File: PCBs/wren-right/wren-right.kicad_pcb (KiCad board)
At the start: 2 copper layers, 151.7 x 117 mm, 67 parts, among them J1 TRRS_Jack, SW0 Reset, U1 Elite C

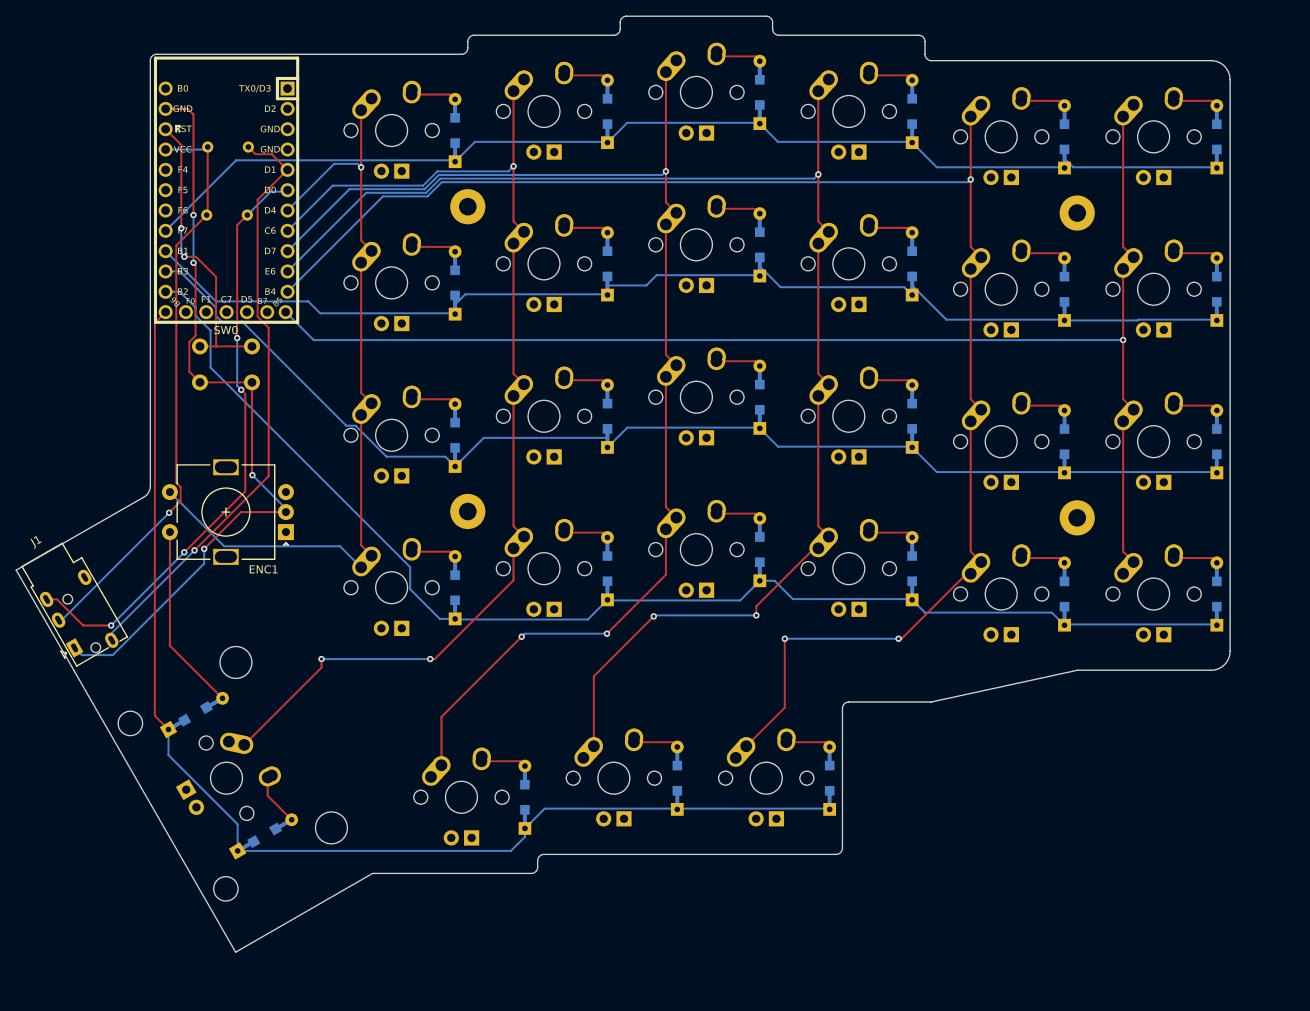
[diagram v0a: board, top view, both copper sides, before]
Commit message: Reposition Rotary Encoder and Create New Right Board
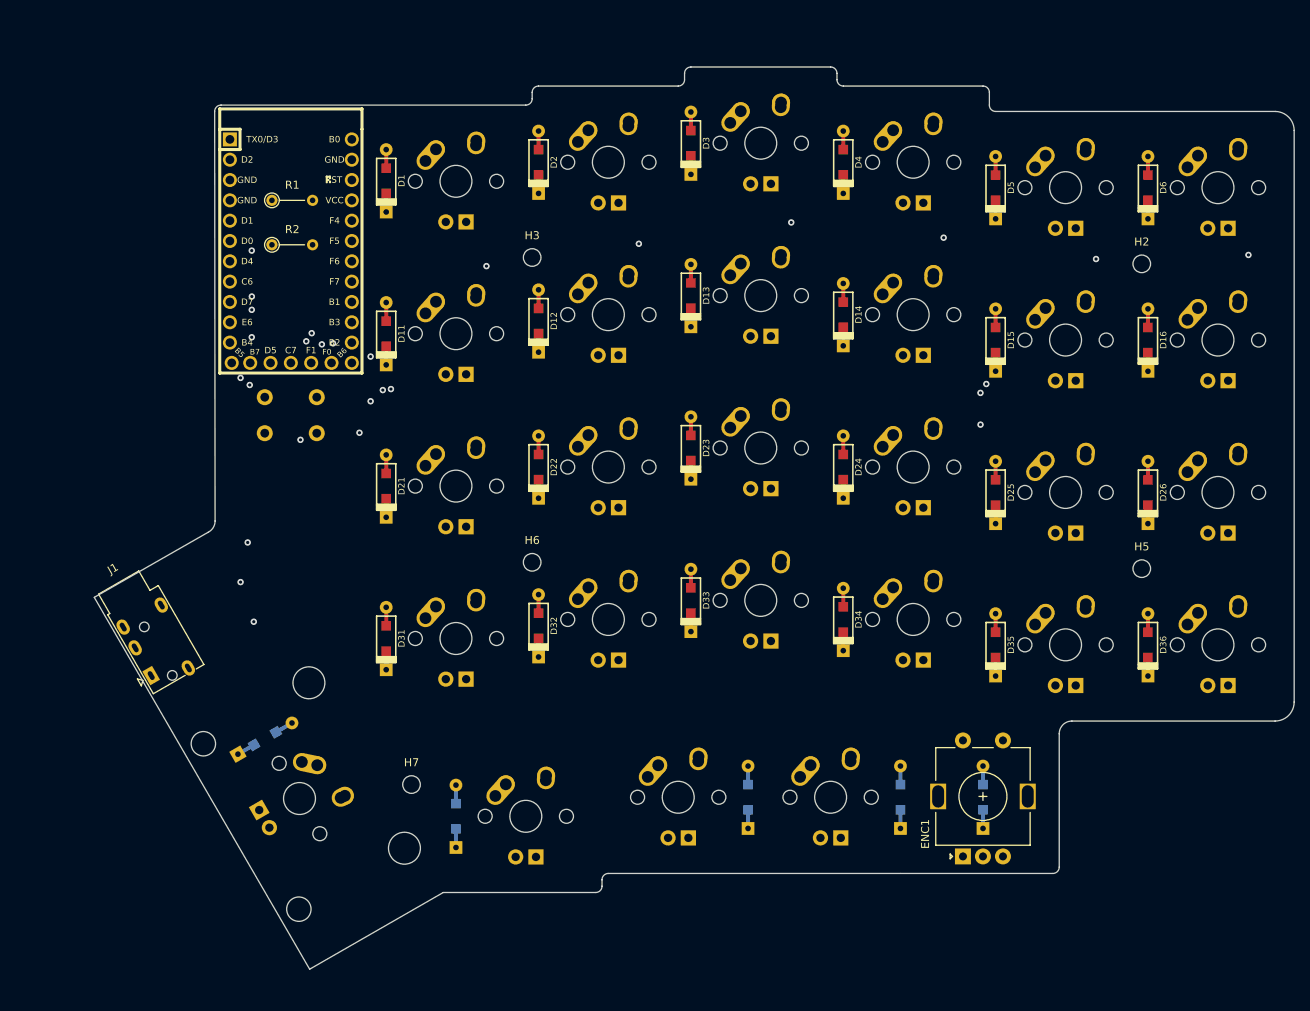
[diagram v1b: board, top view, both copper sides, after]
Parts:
- removed REF** (x4): MountingHole_2.2mm_M2_Pad, MountingHole:MountingHole_2.2mm_M2_Pad
- added H2: MountingHole, MountingHole:MountingHole_2.2mm_M2_ISO7380, F.Cu at (211.9, 73.0)
- added H3: MountingHole, MountingHole:MountingHole_2.2mm_M2_ISO7380, F.Cu at (135.7, 72.2)
- added H5: MountingHole, MountingHole:MountingHole_2.2mm_M2_ISO7380, F.Cu at (211.9, 111.1)
- added H6: MountingHole, MountingHole:MountingHole_2.2mm_M2_ISO7380, F.Cu at (135.7, 110.3)
- added H7: MountingHole, MountingHole:MountingHole_2.2mm_M2_ISO7380, F.Cu at (120.7, 138.1)
- D1, D11, D12, D13, D14, D15, D16, D2, D21, D22, D23, D24, D25, D26, D3, D31, D32, D33, D34, D35, D36, D4, D5, D6, R1, R2: moved to F.Cu
- U1: value Elite C -> Elite-C; moved to F.Cu
- moved ENC1 93.8 mm to (189.6, 147.1), turned to 90 degrees
- moved D44 28.0 mm to (181.8, 139.7)
- moved D43 27.9 mm to (162.7, 139.7)
- moved D42 24.0 mm to (126.2, 142.1), turned to 90 degrees
- moved D45 19.3 mm to (192.1, 139.7)
- moved D12 11.2 mm to (136.5, 80.2)
- moved D32 11.2 mm to (136.5, 118.3)
- moved D35 10.7 mm to (193.7, 120.7)
- moved D5 10.7 mm to (193.7, 63.5)
- moved D15 10.7 mm to (193.7, 82.5)
- moved D25 10.7 mm to (193.7, 101.6)
- moved D13 10.7 mm to (155.6, 77.0)
- moved D21 10.7 mm to (117.5, 100.8)
- moved D23 10.7 mm to (155.6, 96.0)
- moved D31 10.7 mm to (117.5, 119.9)
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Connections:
- D41 pad 2: ENC1-OUT -> Net-(D41-Pad2)
- D45 pad 2: Net-(D45-Pad2) -> ENC1-IN
- ENC1 pad A: (no net) -> LEFT
- ENC1 pad B: (no net) -> RIGHT
- ENC1 pad S1: COL0 -> ENC1-IN
- ENC1 pad S2: ENC1-OUT -> COL4
- MX41 pad 1: COL1 -> COL0
- MX41 pad 2: Net-(D42-Pad2) -> Net-(D41-Pad2)
- MX42 pad 1: COL2 -> COL1
- MX42 pad 2: Net-(D43-Pad2) -> Net-(D42-Pad2)
- MX43 pad 1: COL3 -> COL2
- MX43 pad 2: Net-(D44-Pad2) -> Net-(D43-Pad2)
- MX44 pad 1: COL4 -> COL3
- MX44 pad 2: Net-(D45-Pad2) -> Net-(D44-Pad2)
- U1 pad 1: (no net) -> ROW0
- U1 pad 10: COL3 -> COL9
- U1 pad 11: COL4 -> Net-(U1-Pad11)
- U1 pad 12: COL5 -> ROW4
- U1 pad 13: ROW4 -> COL0
- U1 pad 14: ROW3 -> COL1
- U1 pad 15: ROW2 -> COL2
- U1 pad 16: ROW1 -> COL3
- U1 pad 17: ROW0 -> COL4
- U1 pad 18: (no net) -> COL5
- U1 pad 19: (no net) -> COL6
- U1 pad 2: (no net) -> ROW1
- U1 pad 20: (no net) -> COL7
- U1 pad 24: (no net) -> Net-(U1-Pad24)
- U1 pad 25: (no net) -> Net-(U1-Pad25)
- U1 pad 26: (no net) -> Net-(U1-Pad26)
- U1 pad 27: (no net) -> Net-(U1-Pad27)
- U1 pad 28: (no net) -> RIGHT
- U1 pad 29: (no net) -> LEFT
- U1 pad 3: (no net) -> Net-(U1-Pad3)
- U1 pad 4: (no net) -> Net-(U1-Pad4)
- U1 pad 7: COL0 -> ROW2
- U1 pad 8: COL1 -> ROW3
- U1 pad 9: COL2 -> COL8
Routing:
- net COL4: track 187.6 -> 0.00 mm, vias 3 -> 1
- net COL3: track 169.9 -> 0.00 mm, vias 3 -> 1
- net COL5: track 160.5 -> 0.00 mm
- net ROW3: track 157.7 -> 0.00 mm
- net COL2: track 153.0 -> 0.00 mm, vias 3 -> 1
- net ROW4: track 149.1 -> 0.00 mm
- net ROW2: track 147.0 -> 0.00 mm, vias 0 -> 1
- net ROW0: track 140.5 -> 0.00 mm
- net ROW1: track 140.3 -> 0.00 mm, vias 0 -> 2
- net COL1: track 132.8 -> 0.00 mm, vias 3 -> 1
- net GND: track 98.0 -> 0.00 mm
- net COL0: track 94.0 -> 0.00 mm
- net SDA: track 75.1 -> 0.00 mm, vias 1 -> 2
- net SCL: track 74.9 -> 0.00 mm, vias 4 -> 3
- net VCC: track 72.9 -> 0.00 mm, vias 1 -> 4
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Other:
- board size 151.7 x 117 mm -> 150 x 112.8 mm

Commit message: Various Updates
New plates, updated routing on the right side, assorted other changes.
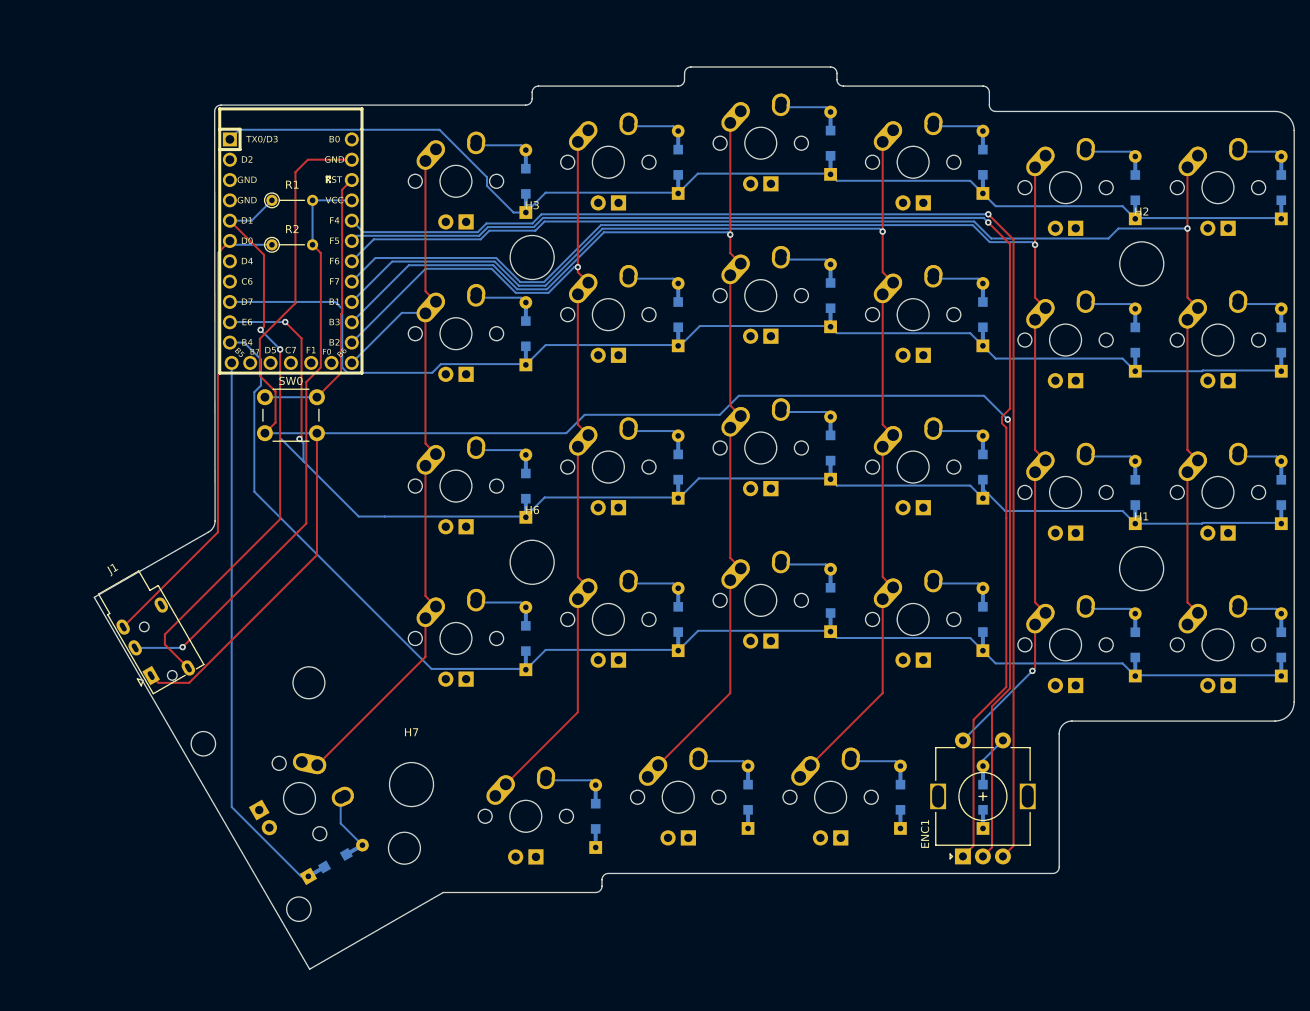
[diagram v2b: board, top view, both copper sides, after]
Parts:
- removed H5: MountingHole, MountingHole:MountingHole_2.2mm_M2_ISO7380
- added H1: MountingHole, MountingHole:MountingHole_5.5mm, F.Cu at (211.9, 111.1)
- D1, D11, D12, D13, D14, D15, D16, D2, D21, D22, D23, D24, D25, D26, D3, D31, D32, D33, D34, D35, D36, D4, D5, D6: moved to B.Cu
- H2, H3, H6, H7: footprint MountingHole:MountingHole_2.2mm_M2_ISO7380 -> MountingHole:MountingHole_5.5mm
- SW0: moved to F.Cu
- moved D41 17.6 mm to (111.1, 147.6)
- moved D12 17.5 mm to (154.0, 79.4)
- moved D32 17.5 mm to (154.0, 117.5)
- moved D42 17.5 mm to (143.7, 142.1)
- moved D1 17.5 mm to (134.9, 62.7)
- moved D15 17.5 mm to (211.1, 82.5)
- moved D25 17.5 mm to (211.1, 101.6)
- moved D35 17.5 mm to (211.1, 120.7)
- moved D5 17.5 mm to (211.1, 63.5)
- moved D11 17.5 mm to (134.9, 81.8)
- moved D13 17.5 mm to (173.0, 77.0)
- moved D14 17.5 mm to (192.1, 79.4)
- moved D2 17.5 mm to (154.0, 60.3)
- moved D21 17.5 mm to (134.9, 100.8)
- moved D22 17.5 mm to (154.0, 98.4)
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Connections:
- U1 pad 10: COL9 -> ROW2
- U1 pad 11: Net-(U1-Pad11) -> ROW3
- U1 pad 19: COL6 -> LEFT
- U1 pad 2: ROW1 -> (no net)
- U1 pad 20: COL7 -> RIGHT
- U1 pad 24: Net-(U1-Pad24) -> (no net)
- U1 pad 25: Net-(U1-Pad25) -> (no net)
- U1 pad 26: Net-(U1-Pad26) -> (no net)
- U1 pad 27: Net-(U1-Pad27) -> (no net)
- U1 pad 28: RIGHT -> (no net)
- U1 pad 29: LEFT -> (no net)
- U1 pad 3: Net-(U1-Pad3) -> (no net)
- U1 pad 4: Net-(U1-Pad4) -> (no net)
- U1 pad 7: ROW2 -> (no net)
- U1 pad 8: ROW3 -> (no net)
- U1 pad 9: COL8 -> ROW1
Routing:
- net GND: track 0.00 -> 238.6 mm, vias 4 -> 1
- net COL4: track 0.00 -> 164.5 mm, vias 1 -> 2
- net LEFT: track 0.00 -> 164.2 mm, vias 2 -> 1
- net ROW3: track 0.00 -> 163.7 mm
- net RIGHT: track 0.00 -> 163.2 mm, vias 2 -> 1
- net COL5: track 0.00 -> 162.3 mm
- net ROW2: track 0.00 -> 159.7 mm, vias 1 -> 2
- net COL3: track 0.00 -> 151.7 mm
- net ROW1: track 0.00 -> 144.5 mm, vias 2 -> 0
- net ROW0: track 0.00 -> 141.4 mm
- net COL2: track 0.00 -> 135.9 mm
- net COL1: track 0.00 -> 115.9 mm
- net COL0: track 0.00 -> 90.2 mm, vias 1 -> 0
- net VCC: track 0.00 -> 74.3 mm, vias 4 -> 1
- net SDA: track 0.00 -> 72.4 mm
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
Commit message: Add Wren Logo (Pt. 2)
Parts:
- added G***: LOGO, footprints:wren_logo, F.Cu at (105.6, 104.8)
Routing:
- net ROW4: track 68.7 -> 155.7 mm

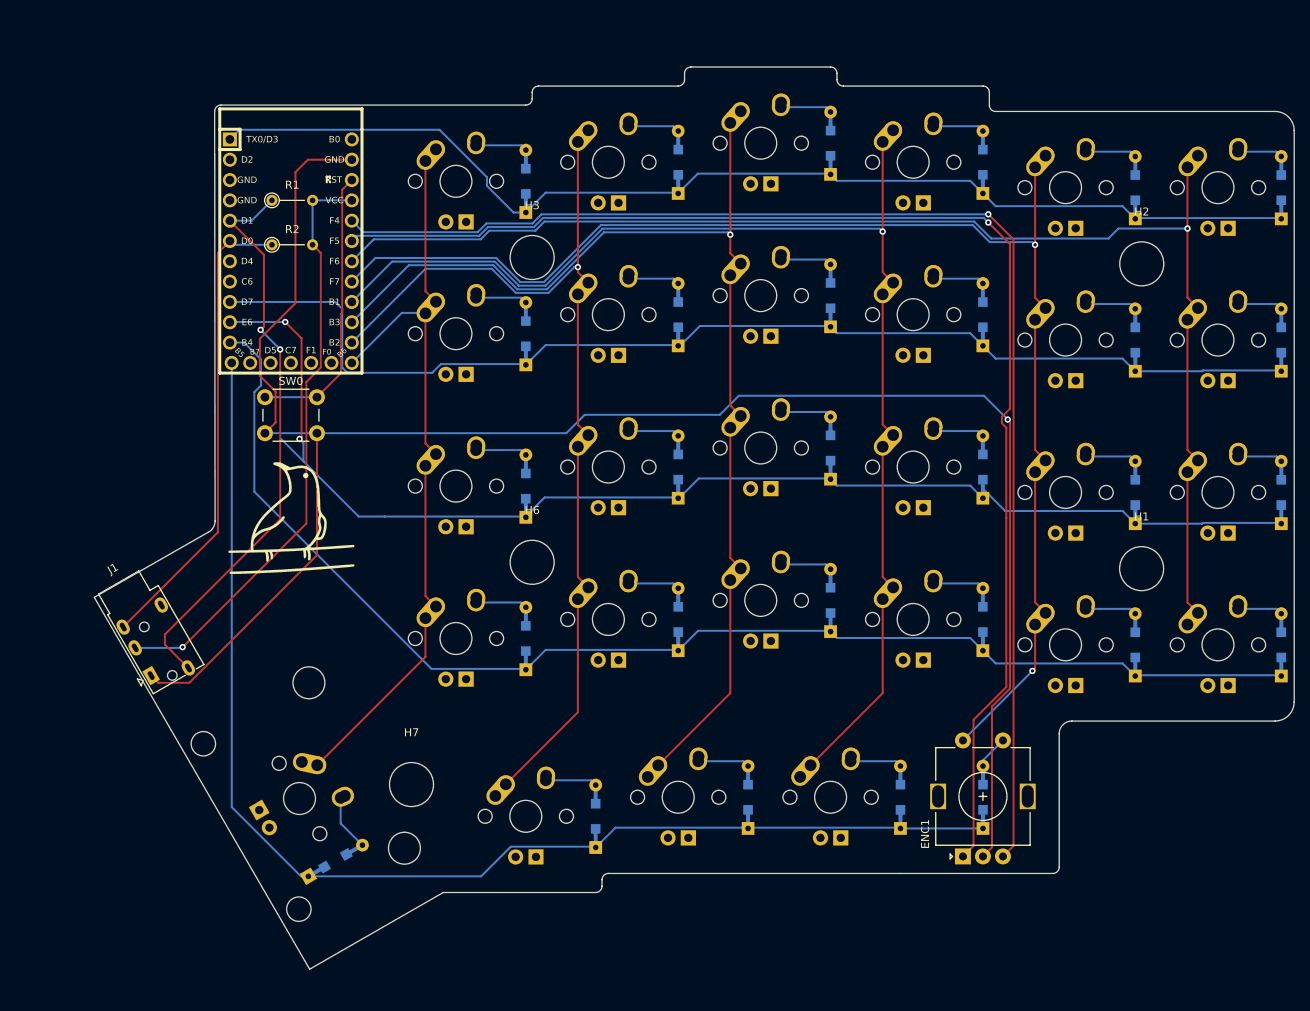
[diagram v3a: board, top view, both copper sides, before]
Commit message: Add increased stagger to right side
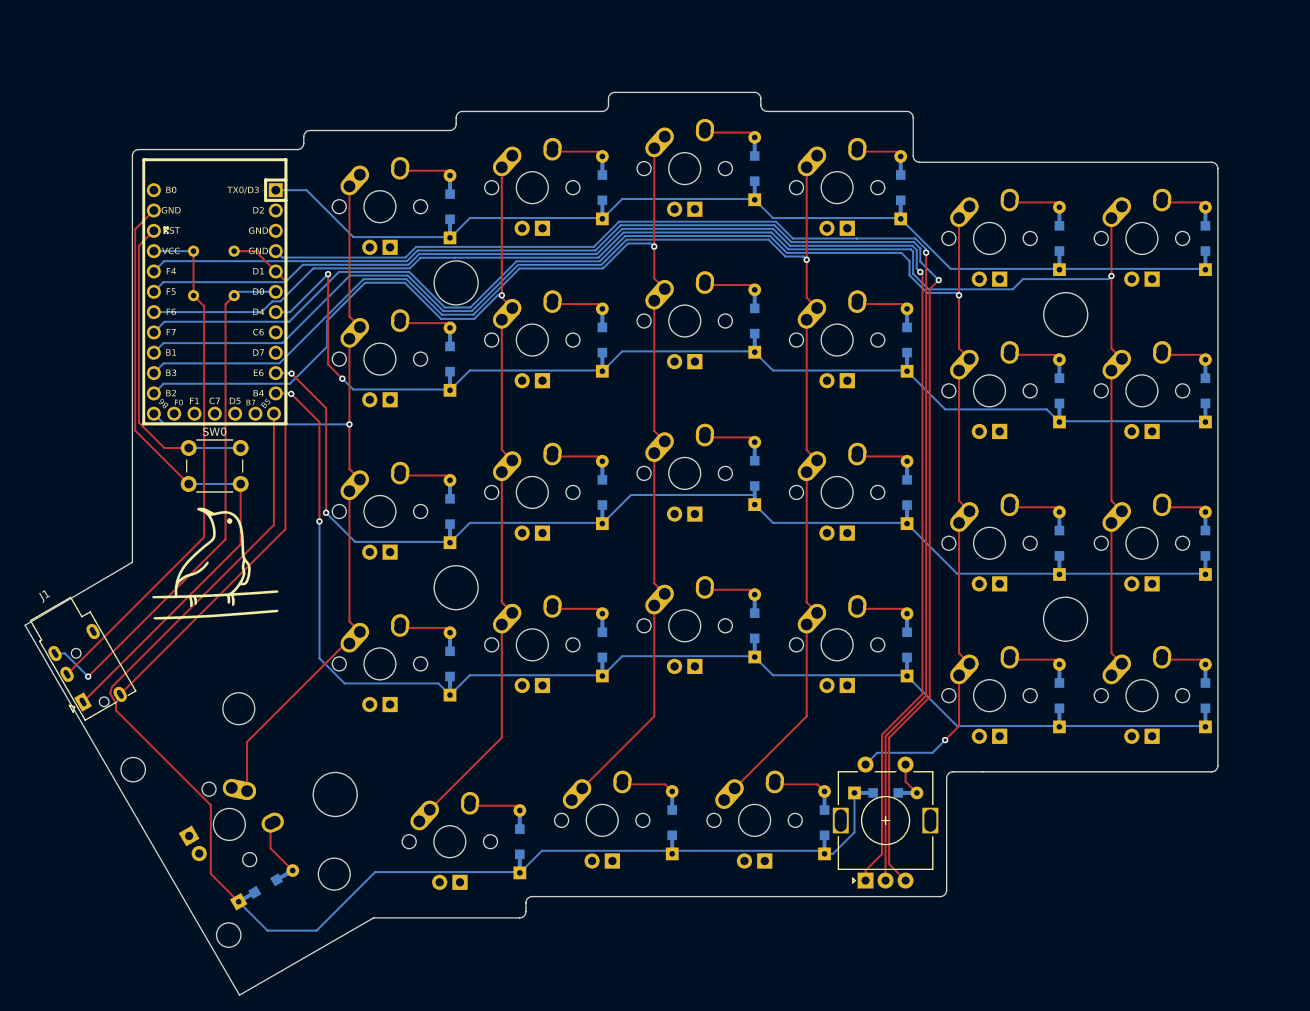
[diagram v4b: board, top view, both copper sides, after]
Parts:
- H1, H2, H3, H6, H7, R1, R2, U1: moved to B.Cu
- moved ENC1 12.5 mm to (177.4, 150.1)
- moved D45 12.2 mm to (179.9, 139.2), turned to 0 degrees
- moved SW0 11.5 mm to (92.8, 96.0)
- moved MX15 11.4 mm to (192.9, 88.9)
- moved MX16 11.4 mm to (212.0, 88.9)
- moved MX25 11.4 mm to (192.9, 108.0)
- moved MX26 11.4 mm to (212.0, 108.0)
- moved H2 11.4 mm to (202.4, 79.4), turned to 180 degrees
- moved MX35 11.4 mm to (192.9, 127.0)
- moved MX36 11.4 mm to (212.0, 127.0)
- moved MX5 11.4 mm to (192.9, 69.8)
- moved MX6 11.4 mm to (212.0, 69.8)
- moved U1 11.4 mm to (96.1, 77.8)
- moved H1 11.4 mm to (202.4, 117.4), turned to 180 degrees
- moved D15 11.4 mm to (201.6, 88.9)
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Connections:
- U1 pad 3: (no net) -> GND
- U1 pad 4: (no net) -> GND
- U1 pad 7: (no net) -> ROW1
- U1 pad 9: ROW1 -> (no net)
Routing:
- net COL4: track 164.5 -> 187.9 mm
- net COL5: track 162.3 -> 183.5 mm
- net ROW2: track 159.7 -> 139.2 mm
- net RIGHT: track 163.2 -> 182.8 mm
- net COL1: track 115.9 -> 135.5 mm
- net COL3: track 151.7 -> 170.8 mm
- net COL2: track 135.9 -> 154.1 mm
- net LEFT: track 164.2 -> 181.8 mm
- net ROW0: track 141.4 -> 124.5 mm
- net COL0: track 90.2 -> 103.4 mm, vias 0 -> 1
- net ROW4: track 155.7 -> 165.2 mm
- net VCC: track 74.3 -> 65.5 mm, vias 1 -> 0
- net ROW3: track 163.7 -> 154.9 mm, vias 0 -> 2
- net ROW1: track 144.5 -> 136.6 mm, vias 0 -> 2
- net GND: track 238.6 -> 245.8 mm
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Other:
- board size 150 x 112.8 mm -> 149.1 x 112.8 mm
